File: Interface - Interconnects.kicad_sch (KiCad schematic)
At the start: 57 parts, among them J10 SM06B-GHS-TB, J11 PTH 01x03 2.54mm, J12 Nano-Fit 1x03, J13 Nano-Fit 1x03, J14 SM05B-GHS-TB, J6 SM08B-GHS-TB, J7 SM07B-GHS-TB, J8 S2B-PH-SM4-TB, J9 S2B-PH-SM4-TB, SW1 CAS-220TA

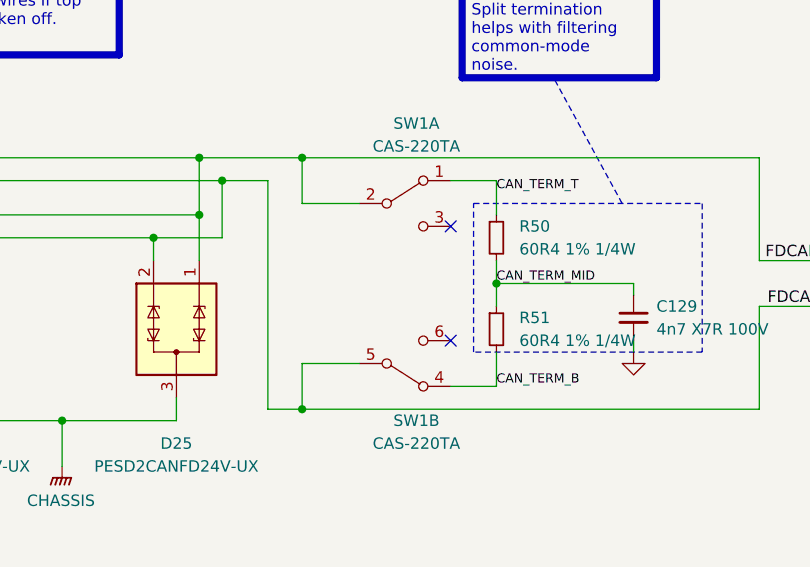
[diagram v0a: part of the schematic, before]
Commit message: Updated files without navigate_results
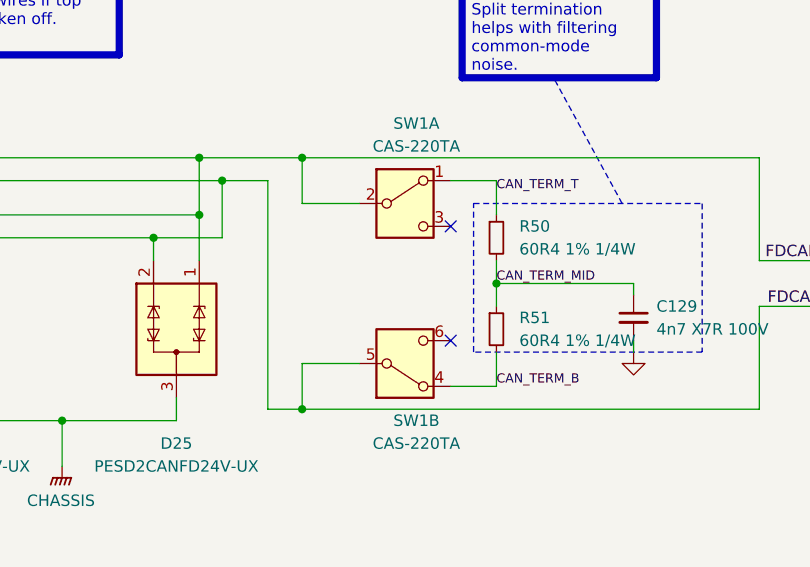
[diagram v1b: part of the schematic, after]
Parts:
- C112, C113, C114, C115, C125, C126, C127, C128: Manufacturer (none) -> Murata Electronics; Manufacturer Part Number (none) -> GCM155R71H104KE02J; manf Murata Electronics -> (none); manf# GCM155R71H104KE02J -> (none)
- C116, C117, C118, C119, C120, C121, C122, C123, C124: Manufacturer (none) -> Murata Electronics; Manufacturer Part Number (none) -> GRM155R72A332KA01D; manf Murata Electronics -> (none); manf# GRM155R72A332KA01D -> (none)
- C129: Manufacturer (none) -> Murata Electronics; Manufacturer Part Number (none) -> GCM155R72A472KA37D; manf Murata Electronics -> (none); manf# GCM155R72A472KA37D -> (none)
- D16, D17: Manufacturer (none) -> Nexperia USA Inc.; Manufacturer Part Number (none) -> PESD4USB5B-TBSX; manf Nexperia USA Inc. -> (none); manf# PESD4USB5B-TBSX -> (none)
- D18, D26: Manufacturer (none) -> Nexperia USA Inc.; Manufacturer Part Number (none) -> PESD4USB3U-TBSX; manf Nexperia USA Inc. -> (none); manf# PESD4USB3U-TBSX -> (none)
- D19, D20, D21, D22: Manufacturer (none) -> STMicroelectronics; Manufacturer Part Number (none) -> BAT41KFILM; manf STMicroelectronics -> (none); manf# BAT41KFILM -> (none)
- D23, D27: Manufacturer (none) -> Bourns Inc.; Manufacturer Part Number (none) -> CDSOT23-SM712; manf Bourns Inc. -> (none); manf# CDSOT23-SM712 -> (none)
- D24, D25: Manufacturer (none) -> Nexperia USA Inc.; Manufacturer Part Number (none) -> PESD2CANFD24V-UX; manf Nexperia USA Inc. -> (none); manf# PESD2CANFD24V-UX -> (none)
- J10: Manufacturer (none) -> JST Sales America Inc.; Manufacturer Part Number (none) -> SM06B-GHS-TB; manf JST Sales America Inc. -> (none); manf# SM06B-GHS-TB -> (none)
- J12, J13: Manufacturer (none) -> Molex; Manufacturer Part Number (none) -> 1054301203; manf Molex -> (none); manf# 1054301203 -> (none)
- J14: Manufacturer (none) -> JST Sales America Inc.; Manufacturer Part Number (none) -> SM05B-GHS-TB; manf JST Sales America Inc. -> (none); manf# SM05B-GHS-TB -> (none)
- J6: Manufacturer (none) -> JST Sales America Inc.; Manufacturer Part Number (none) -> SM08B-GHS-TB; manf JST Sales America Inc. -> (none); manf# SM08B-GHS-TB -> (none)
- J7: Manufacturer (none) -> JST Sales America Inc.; Manufacturer Part Number (none) -> SM07B-GHS-TB(LF)(SN); manf JST Sales America Inc. -> (none); manf# SM07B-GHS-TB(LF)(SN) -> (none)
- J8, J9: Manufacturer (none) -> JST Sales America Inc.; Manufacturer Part Number (none) -> S2B-PH-SM4-TB; manf JST Sales America Inc. -> (none); manf# S2B-PH-SM4-TB -> (none)
- R35, R36, R37, R38, R39, R40, R41, R42, R43, R48, R49: Manufacturer (none) -> Vishay; Manufacturer Part Number (none) -> RCS0402100RFKED; manf Vishay -> (none); manf# RCS0402100RFKED -> (none)
- R44, R45, R46, R47: Manufacturer (none) -> Vishay; Manufacturer Part Number (none) -> ERJ-2RKF2001X; manf Vishay -> (none); manf# ERJ-2RKF2001X -> (none)
- R50, R51: Manufacturer (none) -> Rohm Semiconductor; Manufacturer Part Number (none) -> ESR03EZPF60R4; manf Rohm Semiconductor -> (none); manf# ESR03EZPF60R4 -> (none)
- SW1: Manufacturer (none) -> Nidec Components Corporation; Manufacturer Part Number (none) -> CAS-220TA; manf Nidec Components Corporation -> (none); manf# CAS-220TA -> (none)
